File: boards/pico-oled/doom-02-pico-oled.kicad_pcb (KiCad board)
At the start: 2 copper layers, 150 x 62 mm, 19 parts, among them SW9 JS102011SAQN, U1 SC0915

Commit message: PCBKit's mark and pcbkit.io on every board; the RP2350 handheld ready to order
The handheld runs from two 18650 cells in parallel behind a DW01A protector and a reverse-cell
P-MOSFET, charged at up to 500 mA from the Pico's USB-C by a BQ24075 (power path into VSYS, timers
off for 6 Ah), with an on/off switch on 3V3_EN, M3 holes, ground pours and the console on pads.
Every assembled part has a JLCPCB code in stock (Basic where there is one); the module sockets are
in the BOM, the modules listed in the order's README. Check complete, the ready review clean.
Every board: routed and checked complete with the new mark.
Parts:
- added logo: , Logo_PCBKit_pcbkit.io, F.Cu at (127.8, 195.2)
- SW1, SW2, SW3, SW4, SW5, SW6, SW7, SW8: value (none) -> PTS645SM43SMTR92 LFS

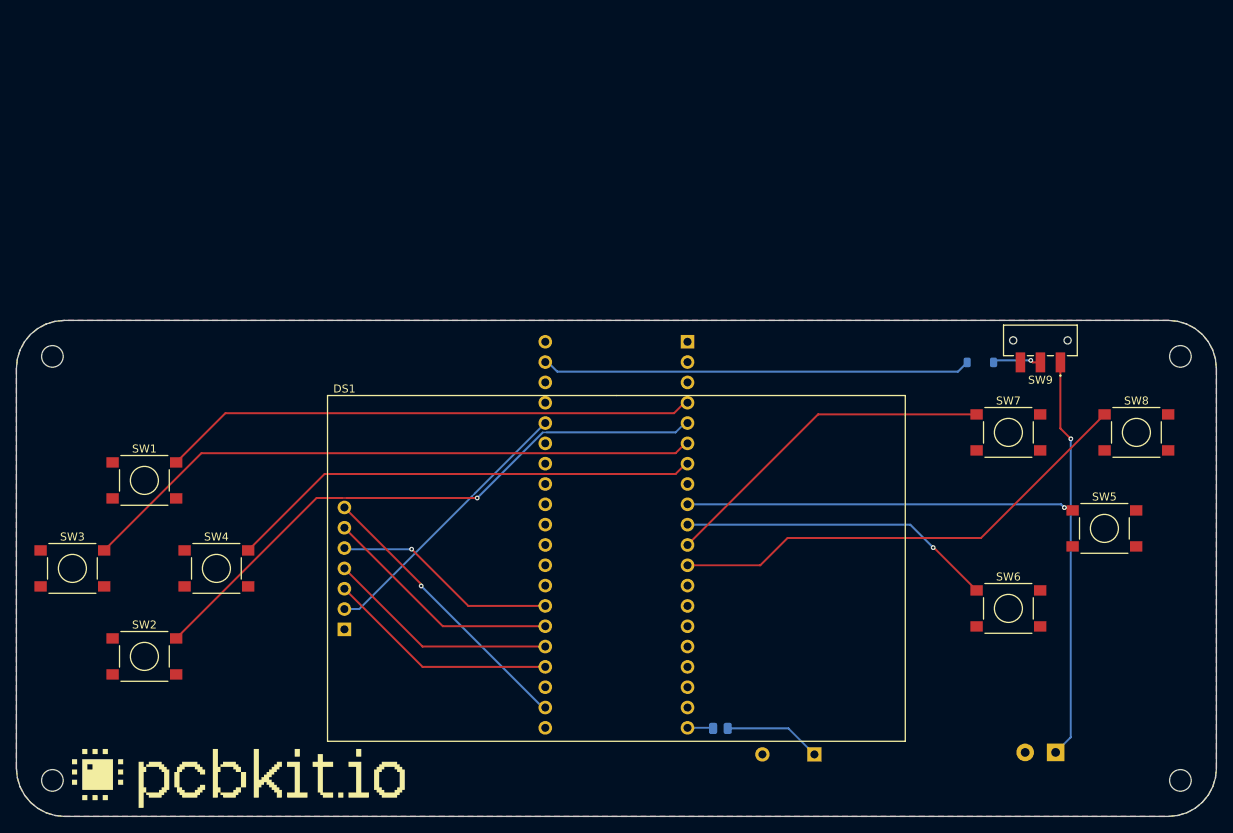
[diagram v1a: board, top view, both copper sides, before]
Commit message: pico-oled: two 18650 cells with protection and a USB charger; every part orderable
Three AA cells become two 18650 in parallel (Keystone 1042 holders on the back) behind a
reverse-cell P-FET and DW01A + FS8205A protection, charged by a BQ24075 with power path from the
Pico's USB (as boards/rp2350-handheld). Board 150 x 100 mm, M3 holes, test pads; every assembled
part pinned to an LCSC code; the README says how to charge and flash.
check: complete, 0 errors, 0 warnings; ready lens: nothing to fix; fab export without --force.

Claude-Session: https://claude.ai/code/session_01ATmMmxyrWxFwR3nTdXUrcx
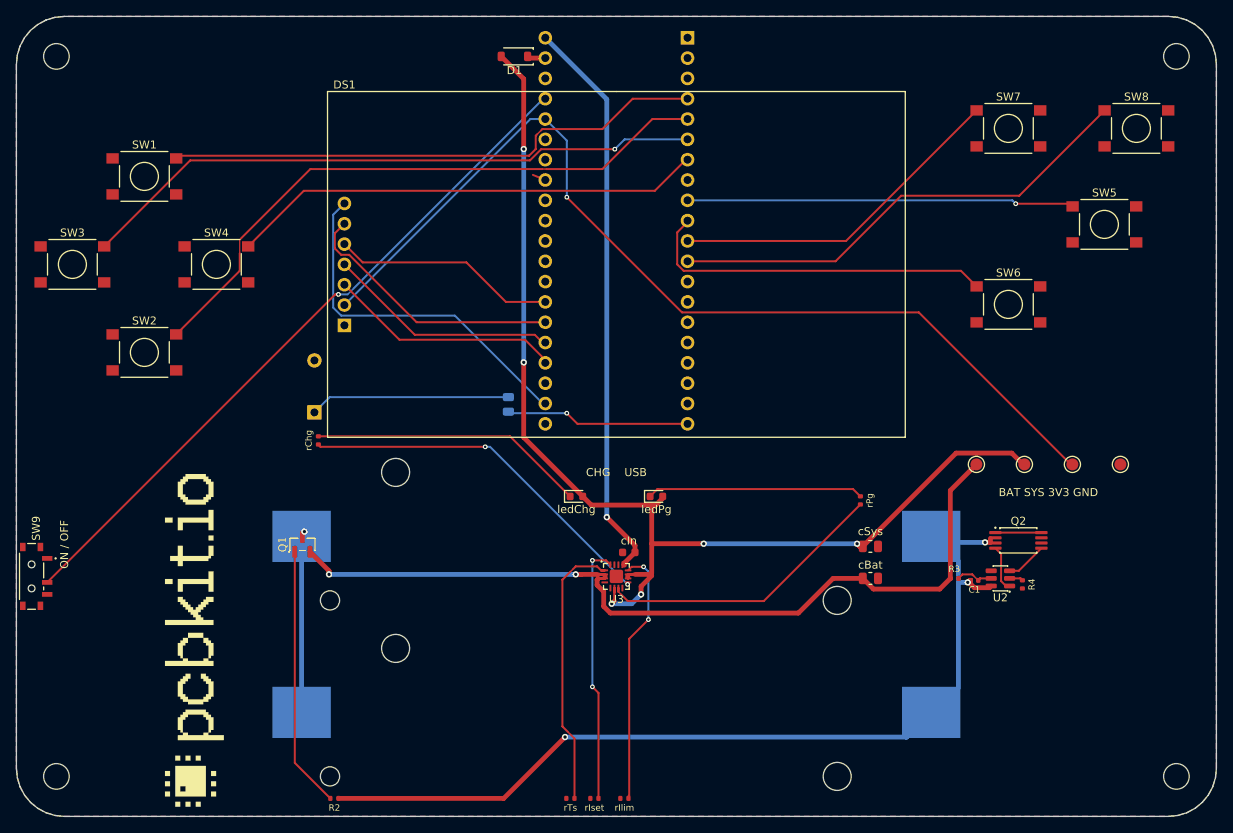
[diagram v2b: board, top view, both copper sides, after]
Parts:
- added BT2: 1042, BatteryHolder_Keystone_1042_1x18650, B.Cu at (175.0, 165.0)
- added C1: 100nF, C_0402_1005Metric, F.Cu at (219.8, 170.5)
- added Q1: AO3401A, SOT-23, F.Cu at (135.8, 166.0)
- added Q2: FS8205A, TSSOP-8_4.4x2.93mm_P0.65mm, F.Cu at (225.2, 165.5)
- added R2: 100kohm, R_0402_1005Metric, F.Cu at (139.8, 197.8)
- added R3: 100ohm, R_0402_1005Metric, F.Cu at (217.2, 170.2)
- added R4: 1kohm, R_0402_1005Metric, F.Cu at (225.8, 171.0)
- added U2: DW01A, SOT-6_1.6x2.9mm_P0.95mm, F.Cu at (223.0, 170.2)
- added U3: BQ24075RGTR, QFN-16-1EP_3x3mm_P0.5mm_EP1.68x1.68mm, F.Cu at (175.0, 170.0)
- added cBat: 4.7uF, C_0805_2012Metric, F.Cu at (206.8, 170.2)
- added cIn: 1uF, C_0603_1608Metric, F.Cu at (176.6, 167.0)
- added cSys: 4.7uF, C_0805_2012Metric, F.Cu at (206.8, 166.2)
- added ledChg: red, LED_0603_1608Metric, F.Cu at (170.0, 160.0)
- added ledPg: green, LED_0603_1608Metric, F.Cu at (180.0, 160.0)
- added rChg: 1.5kohm, R_0402_1005Metric, F.Cu at (137.8, 153.0)
- added rIlim: 1.18kohm, R_0402_1005Metric, F.Cu at (176.0, 197.8)
- added rIset: 1.13kohm, R_0402_1005Metric, F.Cu at (172.2, 197.8)
- added rPg: 1.5kohm, R_0402_1005Metric, F.Cu at (205.5, 160.5)
- added rTs: 10kohm, R_0402_1005Metric, F.Cu at (169.2, 197.8)
- added tpBat: , TestPoint_Round_D1.5mm, F.Cu at (220.0, 156.0)
- added tpGnd: , TestPoint_Round_D1.5mm, F.Cu at (238.0, 156.0)
- added tpSys: , TestPoint_Round_D1.5mm, F.Cu at (226.0, 156.0)
- added tpV3: , TestPoint_Round_D1.5mm, F.Cu at (232.0, 156.0)
- BT1: value 3xAA battery holder with leads -> 1042; footprint BatteryLeads_2x_D1.1mm_P3.81mm -> BatteryHolder_Keystone_1042_1x18650
- D1: value schottky -> 1N5819HW-7-F; moved to F.Cu
- H1, H2, H3, H4: footprint MountingHole_2.7mm_M2.5 -> MountingHole_3.2mm_M3
- SW9: value JS102011SAQN -> MSK12C02; footprint SW_Slide_SPDT_CK_JS102011SAQN_Horizontal -> SW_Slide_SPDT_Shouhan_MSK12C02
- moved SW9 129.5 mm to (101.9, 170.0), turned to 90 degrees
- moved BZ1 75.0 mm to (137.2, 146.2), turned to 270 degrees
- moved D1 69.7 mm to (162.2, 105.0)
- moved BT1 53.2 mm to (175.0, 187.0)
- moved R1 48.4 mm to (161.5, 148.5), turned to 270 degrees
- moved U1 38.0 mm to (175.0, 126.8)
- moved DS1 38.0 mm to (141.0, 131.0)
- moved SW1 38.0 mm to (116.0, 120.0)
- moved SW2 38.0 mm to (116.0, 142.0)
- moved SW3 38.0 mm to (107.0, 131.0)
- moved SW4 38.0 mm to (125.0, 131.0)
- moved SW5 38.0 mm to (236.0, 126.0)
- moved SW6 38.0 mm to (224.0, 136.0)
- moved SW7 38.0 mm to (224.0, 114.0)
- moved SW8 38.0 mm to (240.0, 114.0)
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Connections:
- BT1 pad 1: VBAT -> CELL_N
- BT1 pad 2: GND -> BAT_IN
- D1 pad 2: VSW -> SYS
- SW9 pad 1: VBAT -> GND
- SW9 pad 2: VSW -> PWR_EN
- U1 pad 37: (no net) -> PWR_EN
- U1 pad 40: (no net) -> VBUS
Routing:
- net SYS: track 0.00 -> 150.7 mm, vias 0 -> 6
- net CELL_N: track 0.00 -> 121.3 mm, vias 0 -> 3
- net BAT: track 0.00 -> 108.6 mm, vias 0 -> 2
- net V3: track 34.7 -> 122.7 mm, vias 0 -> 1
- net PWR_EN: track 0.00 -> 87.3 mm, vias 0 -> 1
- net VBUS: track 0.00 -> 71.4 mm, vias 0 -> 1
- net VSYS: track 53.7 -> 2.89 mm
- net VBAT: track 50.1 -> 0.00 mm, vias 1 -> 0
- net CHG_N: track 0.00 -> 46.2 mm, vias 0 -> 2
- net PG_N: track 0.00 -> 37.1 mm
- net TS: track 0.00 -> 35.1 mm
- net CHG_LED: track 0.00 -> 34.6 mm
- net reversed/gate: track 0.00 -> 32.7 mm
- net ISET: track 0.00 -> 32.5 mm, vias 0 -> 2
- net ILIM: track 0.00 -> 32.4 mm, vias 0 -> 2
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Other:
- board size 150 x 62 mm -> 150 x 100 mm
- board text added: "+"
- board text added: "-"
- board text added: "2 x 18650 Li-ion 3.7 V"
- board text added: "BAT SYS 3V3 GND"
- board text added: "CHG USB"
- board text added: "ON / OFF"
